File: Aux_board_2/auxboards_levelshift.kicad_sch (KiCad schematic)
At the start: 5 parts, among them Q1 BSS138KJ, Q2 BSS84KJ

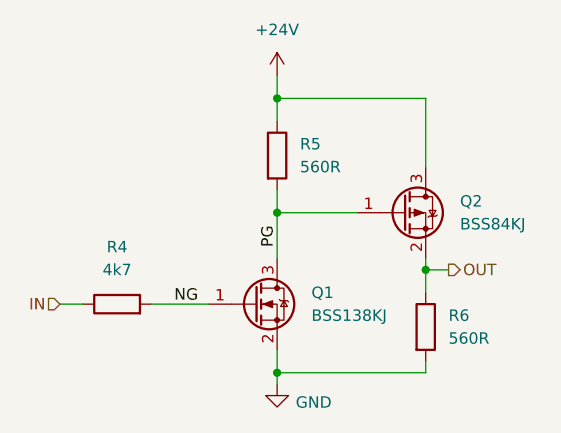
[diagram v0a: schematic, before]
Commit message: Aux Board 2 finished and prod-plotted
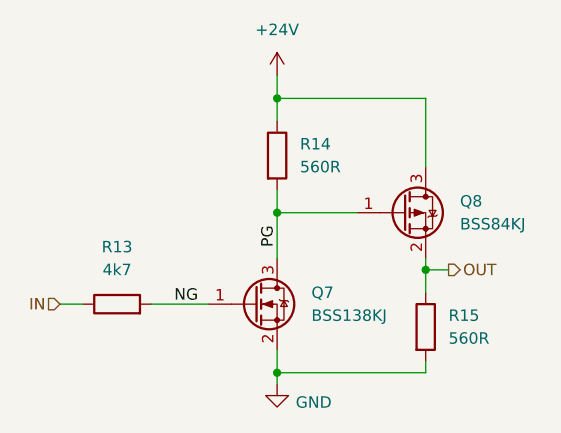
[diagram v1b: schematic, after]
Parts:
- renumbered Q1 to Q7, Q2 to Q8, R4 to R13, R5 to R14, R6 to R15
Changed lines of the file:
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@@
 		(dnp no)
 		(fields_autoplaced yes)
-		(property "Reference" "R4"
+		(property "Reference" "R13"
 			(at 120.65 95.25 90)
 			(effects
@@
 		(instances
 			(project "Aux_board_2"
+				(path "/4ad4dcaf-a806-4024-b268-e11ca8819983/b68f9a89-587f-4950-99af-37e75f787e11"
+					(reference "R13")
+					(unit 1)
+				)
+				(path "/4ad4dcaf-a806-4024-b268-e11ca8819983/9d93e654-f321-40fc-9fa1-2be221aab357"
+					(reference "R16")
+					(unit 1)
+				)
+				(path "/4ad4dcaf-a806-4024-b268-e11ca8819983/09cac996-7c5e-4df3-9a0e-dd5a796db8dc"
+					(reference "R19")
+					(unit 1)
+				)
+				(path "/4ad4dcaf-a806-4024-b268-e11ca8819983/7f43ac15-34e3-4cc6-be87-53fa2a32300c"
+					(reference "R22")
+					(unit 1)
+				)
 				(path "/4ad4dcaf-a806-4024-b268-e11ca8819983/a626a529-b0e7-4337-b470-510e048b53ed"
+					(reference "R10")
+					(unit 1)
+				)
+				(path "/4ad4dcaf-a806-4024-b268-e11ca8819983/ec405cd8-c37b-440f-846d-da22d34634fe"
 					(reference "R4")
 					(unit 1)
 				)
-				(path "/4ad4dcaf-a806-4024-b268-e11ca8819983/0792bb23-301d-463d-a5db-d530de73b851"
+				(path "/4ad4dcaf-a806-4024-b268-e11ca8819983/2b46b460-77b0-4c1b-bab8-59f1ffa8672f"
 					(reference "R7")
 					(unit 1)
@@
 		(on_board yes)
 		(dnp no)
-		(property "Reference" "#PWR023"
+		(property "Reference" "#PWR025"
 			(at 138.43 116.84 0)
 			(effects
@@
 		(instances
 			(project "Aux_board_2"
+				(path "/4ad4dcaf-a806-4024-b268-e11ca8819983/b68f9a89-587f-4950-99af-37e75f787e11"
+					(reference "#PWR025")
+					(unit 1)
+				)
+				(path "/4ad4dcaf-a806-4024-b268-e11ca8819983/9d93e654-f321-40fc-9fa1-2be221aab357"
+					(reference "#PWR027")
+					(unit 1)
+				)
+				(path "/4ad4dcaf-a806-4024-b268-e11ca8819983/09cac996-7c5e-4df3-9a0e-dd5a796db8dc"
+					(reference "#PWR029")
+					(unit 1)
+				)
+				(path "/4ad4dcaf-a806-4024-b268-e11ca8819983/7f43ac15-34e3-4cc6-be87-53fa2a32300c"
+					(reference "#PWR031")
+					(unit 1)
+				)
 				(path "/4ad4dcaf-a806-4024-b268-e11ca8819983/a626a529-b0e7-4337-b470-510e048b53ed"
-					(reference "#PWR023")
-					(unit 1)
-				)
-				(path "/4ad4dcaf-a806-4024-b268-e11ca8819983/0792bb23-301d-463d-a5db-d530de73b851"
+					(reference "#PWR0102")
+					(unit 1)
+				)
+				(path "/4ad4dcaf-a806-4024-b268-e11ca8819983/ec405cd8-c37b-440f-846d-da22d34634fe"
 					(reference "#PWR019")
+					(unit 1)
+				)
+				(path "/4ad4dcaf-a806-4024-b268-e11ca8819983/2b46b460-77b0-4c1b-bab8-59f1ffa8672f"
+					(reference "#PWR021")
 					(unit 1)
 				)
@@
 		(dnp no)
 		(fields_autoplaced yes)
-		(property "Reference" "R5"
+		(property "Reference" "R14"
 			(at 140.97 83.8199 0)
 			(effects
@@
 		(instances
 			(project "Aux_board_2"
+				(path "/4ad4dcaf-a806-4024-b268-e11ca8819983/b68f9a89-587f-4950-99af-37e75f787e11"
+					(reference "R14")
+					(unit 1)
+				)
+				(path "/4ad4dcaf-a806-4024-b268-e11ca8819983/9d93e654-f321-40fc-9fa1-2be221aab357"
+					(reference "R17")
+					(unit 1)
+				)
+				(path "/4ad4dcaf-a806-4024-b268-e11ca8819983/09cac996-7c5e-4df3-9a0e-dd5a796db8dc"
+					(reference "R20")
+					(unit 1)
+				)
+				(path "/4ad4dcaf-a806-4024-b268-e11ca8819983/7f43ac15-34e3-4cc6-be87-53fa2a32300c"
+					(reference "R23")
+					(unit 1)
+				)
 				(path "/4ad4dcaf-a806-4024-b268-e11ca8819983/a626a529-b0e7-4337-b470-510e048b53ed"
+					(reference "R11")
+					(unit 1)
+				)
+				(path "/4ad4dcaf-a806-4024-b268-e11ca8819983/ec405cd8-c37b-440f-846d-da22d34634fe"
 					(reference "R5")
 					(unit 1)
 				)
-				(path "/4ad4dcaf-a806-4024-b268-e11ca8819983/0792bb23-301d-463d-a5db-d530de73b851"
+				(path "/4ad4dcaf-a806-4024-b268-e11ca8819983/2b46b460-77b0-4c1b-bab8-59f1ffa8672f"
 					(reference "R8")
 					(unit 1)
@@
 		(dnp no)
 		(fields_autoplaced yes)
-		(property "Reference" "Q2"
+		(property "Reference" "Q8"
 			(at 158.75 90.1699 0)
 			(effects
@@
 		(instances
 			(project "Aux_board_2"
+				(path "/4ad4dcaf-a806-4024-b268-e11ca8819983/b68f9a89-587f-4950-99af-37e75f787e11"
+					(reference "Q8")
+					(unit 1)
+				)
+				(path "/4ad4dcaf-a806-4024-b268-e11ca8819983/9d93e654-f321-40fc-9fa1-2be221aab357"
+					(reference "Q10")
+					(unit 1)
+				)
+				(path "/4ad4dcaf-a806-4024-b268-e11ca8819983/09cac996-7c5e-4df3-9a0e-dd5a796db8dc"
+					(reference "Q12")
+					(unit 1)
+				)
+				(path "/4ad4dcaf-a806-4024-b268-e11ca8819983/7f43ac15-34e3-4cc6-be87-53fa2a32300c"
+					(reference "Q14")
+					(unit 1)
+				)
 				(path "/4ad4dcaf-a806-4024-b268-e11ca8819983/a626a529-b0e7-4337-b470-510e048b53ed"
+					(reference "Q6")
+					(unit 1)
+				)
+				(path "/4ad4dcaf-a806-4024-b268-e11ca8819983/ec405cd8-c37b-440f-846d-da22d34634fe"
 					(reference "Q2")
 					(unit 1)
 				)
-				(path "/4ad4dcaf-a806-4024-b268-e11ca8819983/0792bb23-301d-463d-a5db-d530de73b851"
+				(path "/4ad4dcaf-a806-4024-b268-e11ca8819983/2b46b460-77b0-4c1b-bab8-59f1ffa8672f"
 					(reference "Q4")
 					(unit 1)
@@
 		(dnp no)
 		(fields_autoplaced yes)
-		(property "Reference" "R6"
+		(property "Reference" "R15"
 			(at 157.48 102.8699 0)
 			(effects
@@
 		(instances
 			(project "Aux_board_2"
+				(path "/4ad4dcaf-a806-4024-b268-e11ca8819983/b68f9a89-587f-4950-99af-37e75f787e11"
+					(reference "R15")
+					(unit 1)
+				)
+				(path "/4ad4dcaf-a806-4024-b268-e11ca8819983/9d93e654-f321-40fc-9fa1-2be221aab357"
+					(reference "R18")
+					(unit 1)
+				)
+				(path "/4ad4dcaf-a806-4024-b268-e11ca8819983/09cac996-7c5e-4df3-9a0e-dd5a796db8dc"
+					(reference "R21")
+					(unit 1)
+				)
+				(path "/4ad4dcaf-a806-4024-b268-e11ca8819983/7f43ac15-34e3-4cc6-be87-53fa2a32300c"
+					(reference "R24")
+					(unit 1)
+				)
 				(path "/4ad4dcaf-a806-4024-b268-e11ca8819983/a626a529-b0e7-4337-b470-510e048b53ed"
+					(reference "R12")
+					(unit 1)
+				)
+				(path "/4ad4dcaf-a806-4024-b268-e11ca8819983/ec405cd8-c37b-440f-846d-da22d34634fe"
 					(reference "R6")
 					(unit 1)
 				)
-				(path "/4ad4dcaf-a806-4024-b268-e11ca8819983/0792bb23-301d-463d-a5db-d530de73b851"
+				(path "/4ad4dcaf-a806-4024-b268-e11ca8819983/2b46b460-77b0-4c1b-bab8-59f1ffa8672f"
 					(reference "R9")
 					(unit 1)
@@
 		(dnp no)
 		(fields_autoplaced yes)
-		(property "Reference" "Q1"
+		(property "Reference" "Q7"
 			(at 142.24 100.3299 0)
 			(effects
@@
 		(instances
 			(project "Aux_board_2"
+				(path "/4ad4dcaf-a806-4024-b268-e11ca8819983/b68f9a89-587f-4950-99af-37e75f787e11"
+					(reference "Q7")
+					(unit 1)
+				)
+				(path "/4ad4dcaf-a806-4024-b268-e11ca8819983/9d93e654-f321-40fc-9fa1-2be221aab357"
+					(reference "Q9")
+					(unit 1)
+				)
+				(path "/4ad4dcaf-a806-4024-b268-e11ca8819983/09cac996-7c5e-4df3-9a0e-dd5a796db8dc"
+					(reference "Q11")
+					(unit 1)
+				)
+				(path "/4ad4dcaf-a806-4024-b268-e11ca8819983/7f43ac15-34e3-4cc6-be87-53fa2a32300c"
+					(reference "Q13")
+					(unit 1)
+				)
 				(path "/4ad4dcaf-a806-4024-b268-e11ca8819983/a626a529-b0e7-4337-b470-510e048b53ed"
+					(reference "Q5")
+					(unit 1)
+				)
+				(path "/4ad4dcaf-a806-4024-b268-e11ca8819983/ec405cd8-c37b-440f-846d-da22d34634fe"
 					(reference "Q1")
 					(unit 1)
 				)
-				(path "/4ad4dcaf-a806-4024-b268-e11ca8819983/0792bb23-301d-463d-a5db-d530de73b851"
+				(path "/4ad4dcaf-a806-4024-b268-e11ca8819983/2b46b460-77b0-4c1b-bab8-59f1ffa8672f"
 					(reference "Q3")
 					(unit 1)
@@
 		(dnp no)
 		(fields_autoplaced yes)
-		(property "Reference" "#PWR022"
+		(property "Reference" "#PWR024"
 			(at 138.43 80.01 0)
 			(effects
@@
 		(instances
 			(project "Aux_board_2"
+				(path "/4ad4dcaf-a806-4024-b268-e11ca8819983/b68f9a89-587f-4950-99af-37e75f787e11"
+					(reference "#PWR024")
+					(unit 1)
+				)
+				(path "/4ad4dcaf-a806-4024-b268-e11ca8819983/9d93e654-f321-40fc-9fa1-2be221aab357"
+					(reference "#PWR026")
+					(unit 1)
+				)
+				(path "/4ad4dcaf-a806-4024-b268-e11ca8819983/09cac996-7c5e-4df3-9a0e-dd5a796db8dc"
+					(reference "#PWR028")
+					(unit 1)
+				)
+				(path "/4ad4dcaf-a806-4024-b268-e11ca8819983/7f43ac15-34e3-4cc6-be87-53fa2a32300c"
+					(reference "#PWR030")
+					(unit 1)
+				)
 				(path "/4ad4dcaf-a806-4024-b268-e11ca8819983/a626a529-b0e7-4337-b470-510e048b53ed"
-					(reference "#PWR022")
-					(unit 1)
-				)
-				(path "/4ad4dcaf-a806-4024-b268-e11ca8819983/0792bb23-301d-463d-a5db-d530de73b851"
+					(reference "#PWR0101")
+					(unit 1)
+				)
+				(path "/4ad4dcaf-a806-4024-b268-e11ca8819983/ec405cd8-c37b-440f-846d-da22d34634fe"
 					(reference "#PWR018")
 					(unit 1)
 				)
+				(path "/4ad4dcaf-a806-4024-b268-e11ca8819983/2b46b460-77b0-4c1b-bab8-59f1ffa8672f"
+					(reference "#PWR020")
+					(unit 1)
+				)
